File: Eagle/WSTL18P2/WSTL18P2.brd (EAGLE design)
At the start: 23.2 x 23.2 mm, 22 parts, among them CON1 1X6CONN-1.27-ROUND, CON2 1X6CONN-1.27-ROUND, CON3 1X6CONN-1.27-ROUND, CON4 1X6CONN-1.27-ROUND, T1 ABS07AIG

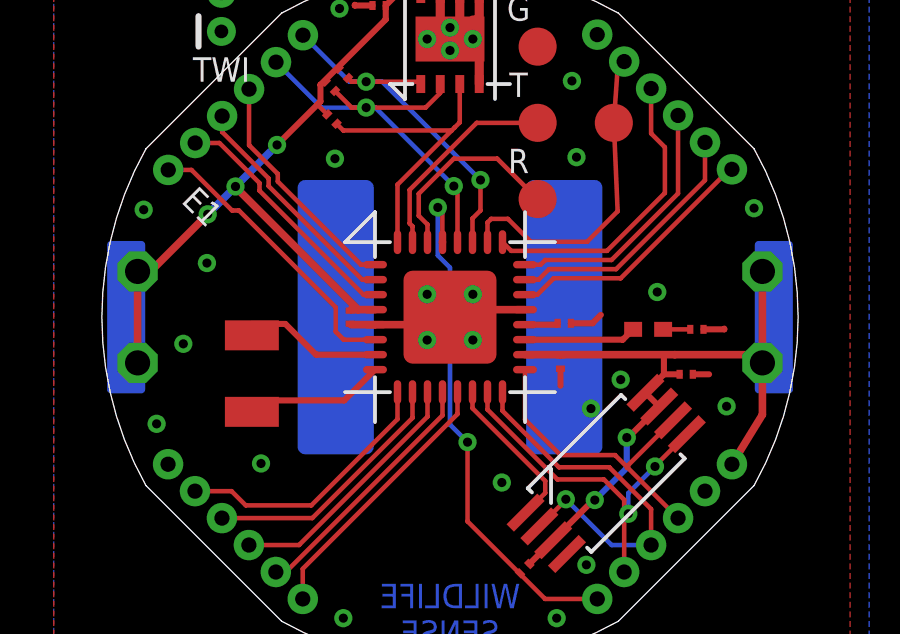
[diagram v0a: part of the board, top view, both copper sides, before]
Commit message: Moved battery GND pad to a sincle circular in centre
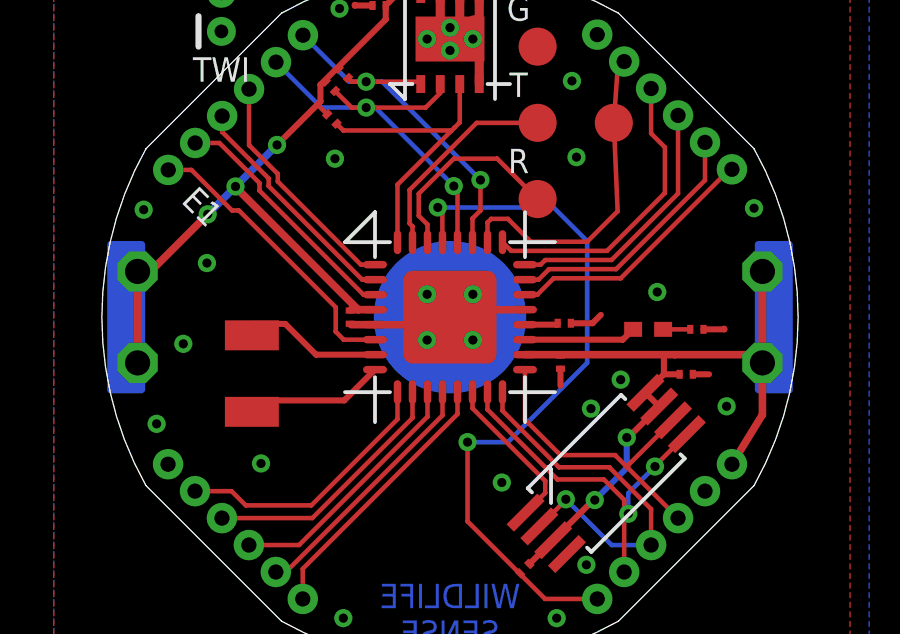
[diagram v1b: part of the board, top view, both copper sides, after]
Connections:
- net GND: no longer U$1.GND1
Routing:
- net RESET: track 17.5 -> 23.9 mm
- net GND: track 15.5 -> 16.1 mm
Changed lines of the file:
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@@
 <wire x1="12.954" y1="15.712" x2="12.954" y2="16.7132" width="0.1524" layer="1"/>
 <via x="12.8016" y="16.8656" extent="1-16" drill="0.3048" shape="octagon"/>
-<wire x1="12.8016" y1="15.2654" x2="13.208" y2="14.859" width="0.1524" layer="16"/>
-<wire x1="12.8016" y1="15.2654" x2="12.8016" y2="16.8656" width="0.1524" layer="16"/>
 <wire x1="12.954" y1="16.7132" x2="12.8016" y2="16.8656" width="0.1524" layer="1"/>
 <wire x1="13.7922" y1="6.4008" x2="15.541634375" y2="4.651365625" width="0.1524" layer="1"/>
@@
 <wire x1="18.115871875" y1="3.815671875" x2="16.377328125" y2="3.815671875" width="0.1524" layer="1"/>
 <wire x1="15.541634375" y1="4.670434375" x2="15.541634375" y2="4.651365625" width="0.1524" layer="1"/>
-<wire x1="13.208" y1="14.859" x2="13.208" y2="9.6266" width="0.1524" layer="16"/>
-<wire x1="13.208" y1="9.6266" x2="13.7922" y2="9.0424" width="0.1524" layer="16"/>
 <via x="13.7922" y="9.0424" extent="1-16" drill="0.3048" shape="octagon"/>
 <wire x1="13.7922" y1="9.0424" x2="13.7922" y2="6.4008" width="0.1524" layer="1"/>
+<wire x1="12.8016" y1="16.8656" x2="16.6624" y2="16.8656" width="0.1524" layer="16"/>
+<wire x1="16.6624" y1="16.8656" x2="17.78" y2="15.748" width="0.1524" layer="16"/>
+<wire x1="17.78" y1="15.748" x2="17.78" y2="11.684" width="0.1524" layer="16"/>
+<wire x1="17.78" y1="11.684" x2="15.1384" y2="9.0424" width="0.1524" layer="16"/>
+<wire x1="15.1384" y1="9.0424" x2="13.7922" y2="9.0424" width="0.1524" layer="16"/>
 </signal>
 <signal name="VCC">
@@
 <contactref element="MCU" pad="PAD"/>
 <wire x1="10.708" y1="12.958" x2="12.446" y2="12.958" width="0.254" layer="1"/>
-<wire x1="12.446" y1="12.958" x2="12.446" y2="12.446" width="0.254" layer="1"/>
 <wire x1="13.97" y1="13.458" x2="13.97" y2="13.97" width="0.254" layer="1"/>
 <via x="6.9088" y="8.3312" extent="1-16" drill="0.3048"/>
@@
 <via x="14.9352" y="7.6962" extent="1-16" drill="0.3048"/>
 <via x="5.1054" y="15.0114" extent="1-16" drill="0.3048"/>
-<contactref element="U$1" pad="GND1"/>
 <contactref element="U$1" pad="GND"/>
 <via x="9.525" y="23.495" extent="1-16" drill="0.3048"/>
@@
 <wire x1="22.352" y1="12.8016" x2="22.352" y2="12.827" width="0.2032" layer="1"/>
 <wire x1="15.708" y1="13.458" x2="13.97" y2="13.458" width="0.254" layer="1"/>
+<wire x1="13.208" y1="13.208" x2="12.446" y2="12.446" width="0.4064" layer="16"/>
+<wire x1="13.208" y1="13.208" x2="13.97" y2="13.458" width="0" layer="19" extent="1-16"/>
+<wire x1="13.208" y1="13.208" x2="13.208" y2="13.208" width="0" layer="19" extent="1-16"/>
+<wire x1="12.446" y1="13.97" x2="12.696" y2="13.208" width="0" layer="19" extent="1-1"/>
+<wire x1="13.97" y1="12.446" x2="13.97" y2="13.458" width="0" layer="19" extent="1-1"/>
 </signal>
 <signal name="AREF">

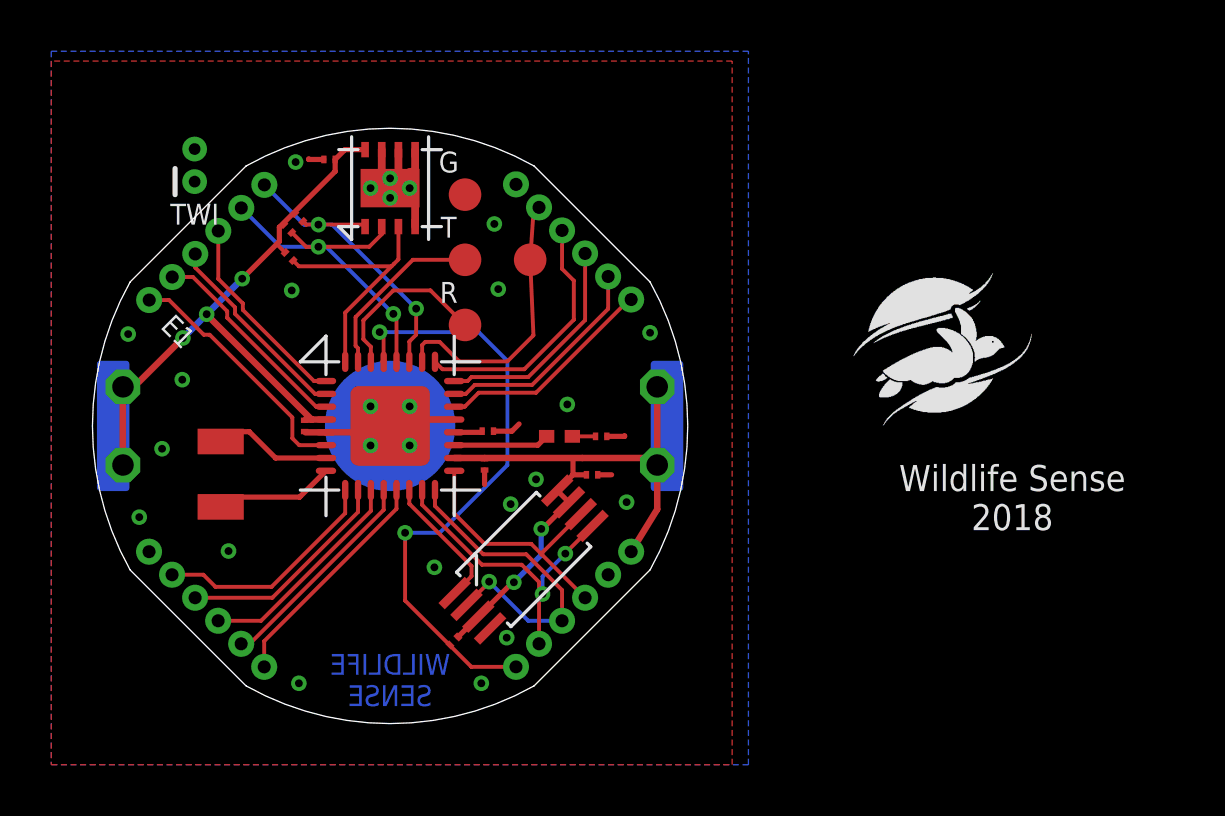
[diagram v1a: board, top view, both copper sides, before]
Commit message: Reverted some passives back to 0402 size
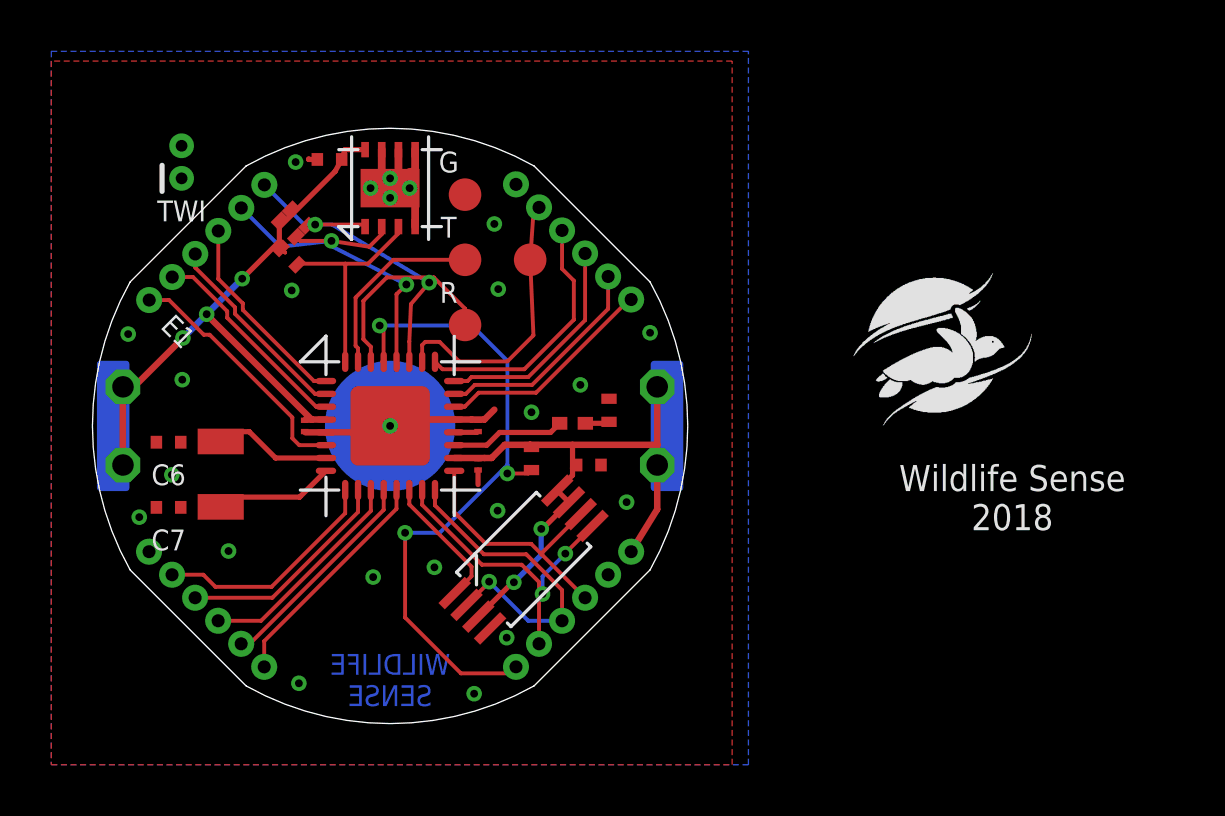
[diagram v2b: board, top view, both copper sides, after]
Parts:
- added C6, C7: CAP_0402_CERAMIC, Passives:CAP_0402
- C4, C5: device Passives:RES_CAP_0201 -> Passives:CAP_0402
- R1, R2, R3, R4, R5: device Passives:RES_CAP_0201 -> Passives:RES_0402
- moved R1 7.73 mm to (18.7, 11.9), turned to 270 degrees
- moved R5 1.06 mm to (21.7, 13.8), turned to 90 degrees
- moved LED0 0.72 mm to (20.3, 13.3)
- moved TWI 0.52 mm to (5.08, 22.9)
- moved C3 0.43 mm to (16.6, 13.2), turned to 90 degrees
- moved C5 0.40 mm to (21.0, 11.7)
- moved C2 0.25 mm to (16.6, 11.7)
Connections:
- net GND: now also C6.2, C7.2
- net N$1: now also C7.1
- net N$2: now also C6.1
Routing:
- net RESET: track 23.9 -> 26.1 mm, vias 2 -> 3
- net TMP_INT: track 10.1 -> 8.62 mm
- net GND: track 16.1 -> 14.8 mm, vias 26 -> 24
- net RXD0: track 6.74 -> 7.98 mm
- net SCL0: track 13.8 -> 14.7 mm
- net SDA0: track 12.6 -> 13.4 mm
- net PE2: track 3.75 -> 4.46 mm
- net VCC: track 49.0 -> 48.3 mm

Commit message: Removed WP and HOLD connections to VCC on EEPROM
Chip has internal pull-ups for when WP and HOLD functions are not used
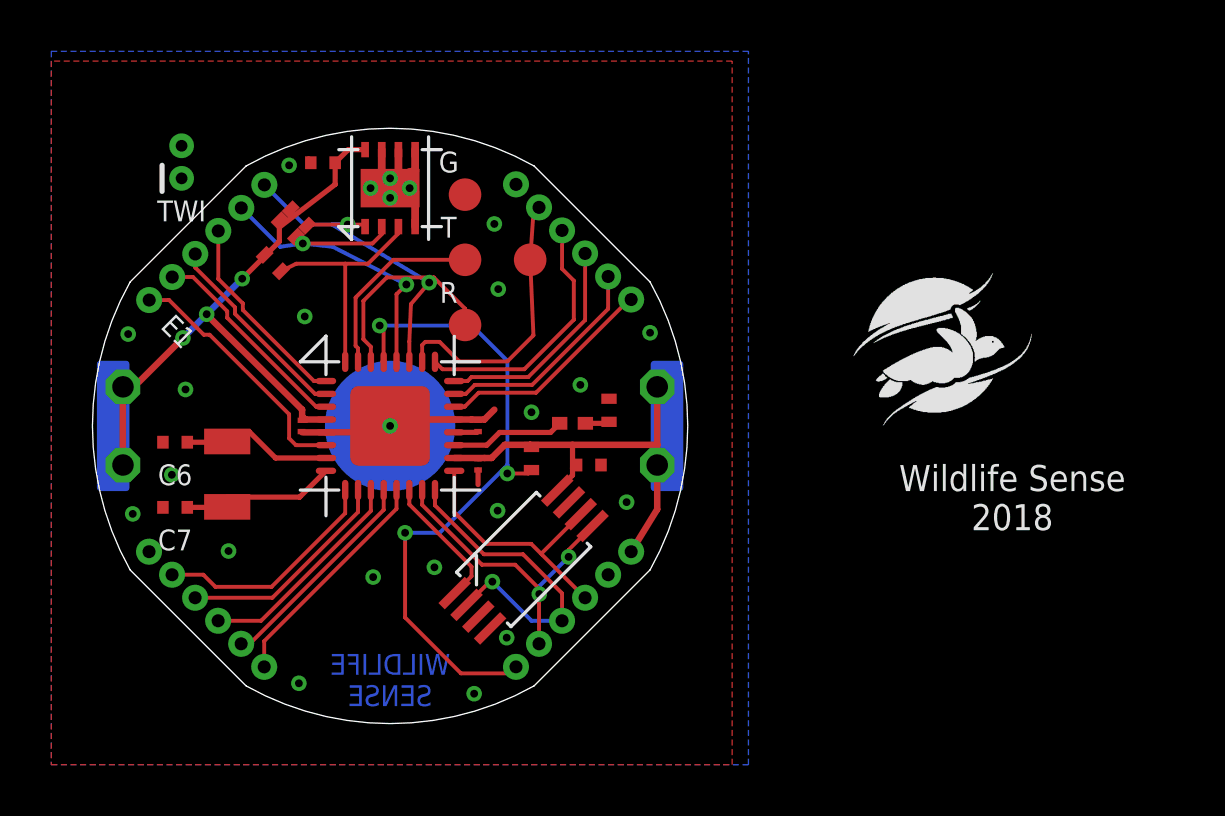
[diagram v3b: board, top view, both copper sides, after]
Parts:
- moved R4 0.68 mm to (8.64, 19.6)
- moved C4 0.28 mm to (10.6, 23.5)
- moved C6 0.25 mm to (4.83, 12.6)
- moved C7 0.25 mm to (4.83, 10.0)
- moved T1 0.25 mm to (6.86, 11.3)
- moved C1 0.13 mm to (9.75, 13.2)
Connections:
- net VCC: no longer MEM.3, MEM.7
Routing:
- net VCC: track 48.3 -> 41.3 mm, vias 5 -> 3
- net N$2: track 4.91 -> 6.22 mm
- net N$1: track 4.91 -> 6.22 mm
- net SDA0: track 13.4 -> 14.6 mm
- net TMP_INT: track 8.62 -> 9.22 mm

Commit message: Rerouted TWI (I2C)
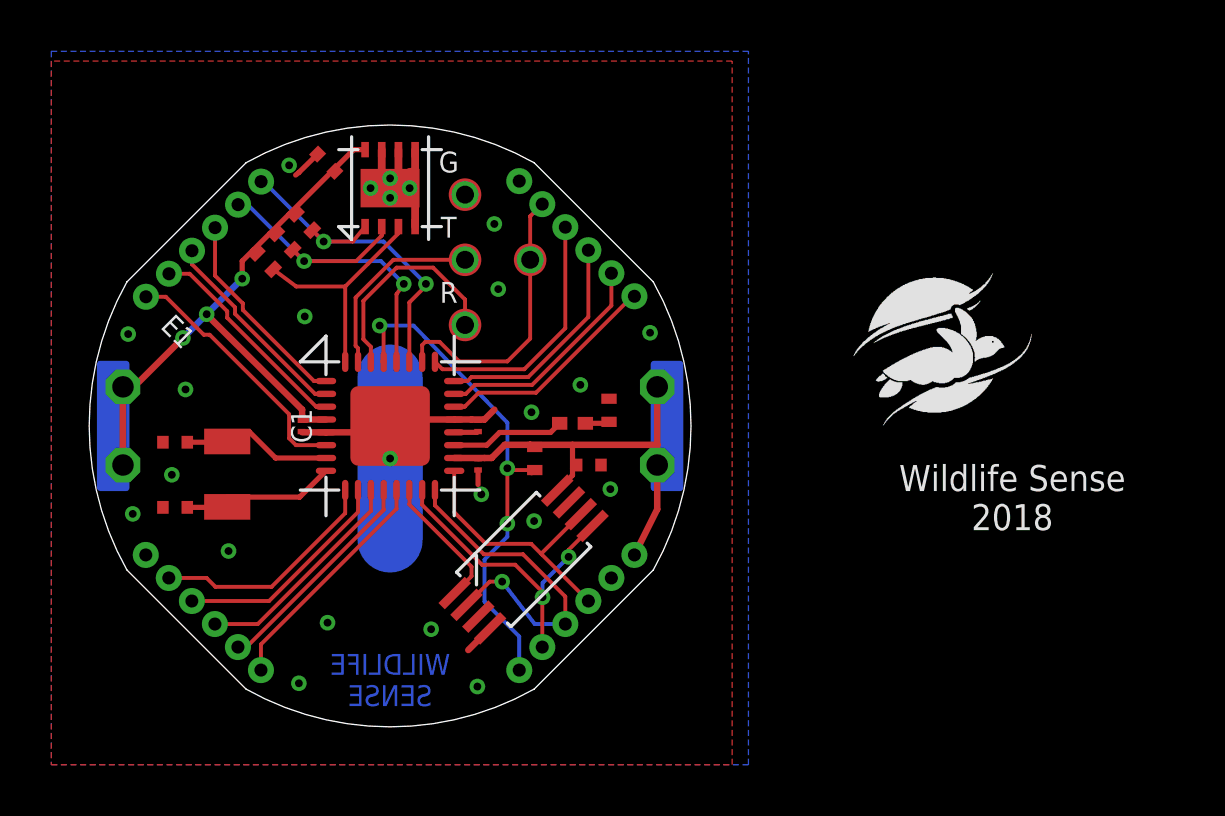
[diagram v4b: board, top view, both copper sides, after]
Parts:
- removed TWI: 1X2CONN1.27, AVR_ISP_127:1X2_1.27
- moved R3 0.52 mm to (9.09, 20.4)
- moved R4 0.31 mm to (8.33, 19.6)
- moved R2 0.27 mm to (9.86, 21.2)
- moved CON2 0.18 mm to (3.68, 8.18)
- moved CON1 0.18 mm to (22.7, 8.18)
- moved CON3 0.18 mm to (22.7, 18.3)
- moved CON4 0.18 mm to (8.18, 22.7)
- moved R1 0.13 mm to (18.8, 11.9)
- moved C4 0.13 mm to (10.7, 23.5), turned to 135 degrees
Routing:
- net RESET: track 26.1 -> 19.9 mm
- net VCC: track 41.3 -> 45.6 mm
- net GND: track 14.7 -> 18.8 mm, vias 24 -> 25
- net SCL0: track 14.5 -> 15.6 mm
- net SDA0: track 14.6 -> 13.9 mm
- net RXD0: track 7.98 -> 8.50 mm, vias 0 -> 1
- net PC3: track 10.9 -> 11.0 mm, vias 0 -> 1
- net TXD0: vias 0 -> 1
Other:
- board size 23.2 x 23.2 mm -> 23.5 x 23.5 mm

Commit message: Eliminated all 0201 passives, changed uart connection pin
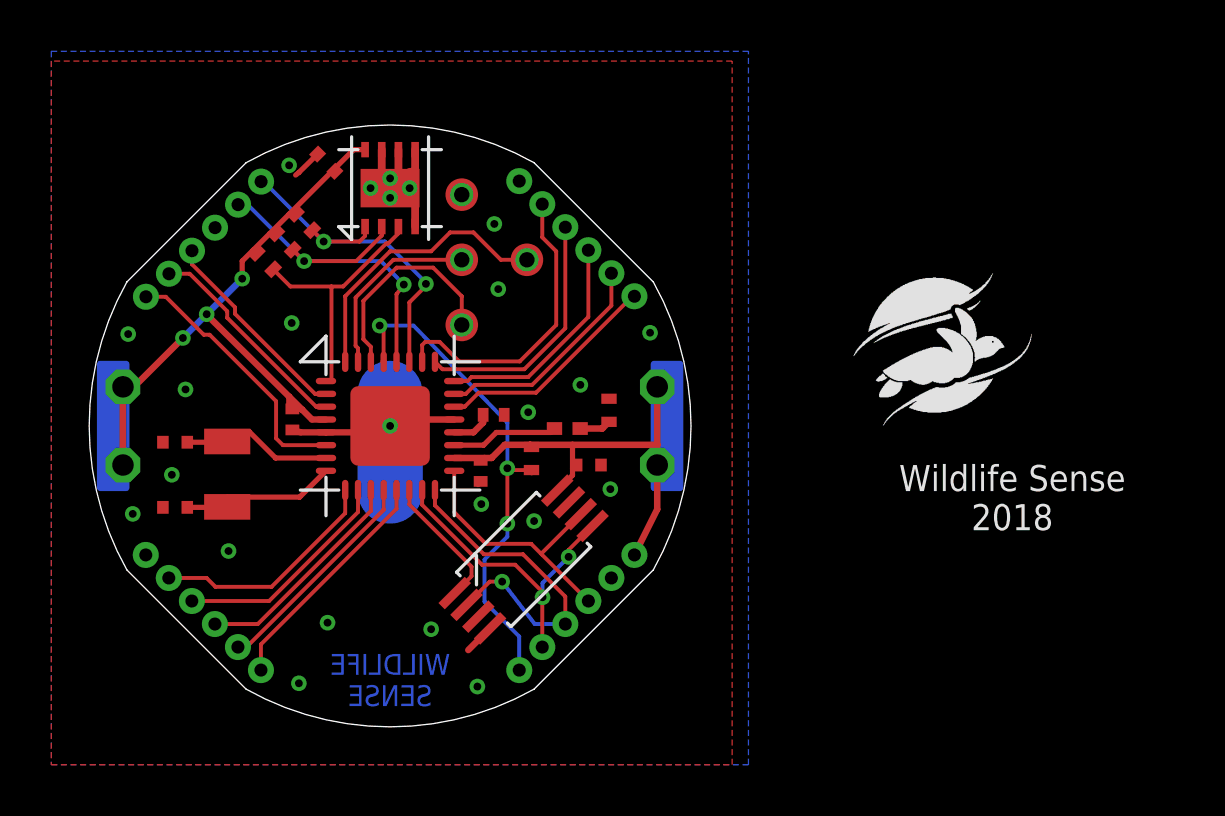
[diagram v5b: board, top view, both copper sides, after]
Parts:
- C1, C2, C3: device Passives:RES_CAP_0201 -> Passives:SMD_0402
- moved C3 0.75 mm to (17.2, 13.6)
- moved C1 0.44 mm to (9.40, 13.5), turned to 0 degrees
- moved LED0 0.29 mm to (20.1, 13.1)
- moved C2 0.27 mm to (16.7, 11.5), turned to 0 degrees
- moved R1 0.13 mm to (18.7, 11.9)
- moved UART 0.13 mm to (16.0, 17.1)
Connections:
- removed net PD3: CON4.3, MCU.1
- new net PD2: MCU.32, UART.1
- new net UNKN1: CON4.3
- net PC3: no longer UART.1
- net TMP_INT: now also MCU.1; no longer MCU.32
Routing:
- net PD2: track 0.00 -> 11.1 mm, vias 0 -> 1
- net PD3: track 8.05 -> 0.00 mm
- net GND: track 18.8 -> 14.7 mm
- net TMP_INT: track 9.16 -> 10.2 mm
- net PC3: track 11.0 -> 11.8 mm, vias 1 -> 0
- net AREF: track 0.94 -> 1.59 mm
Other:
- board text removed: "E1"
- board text removed: "G"
- board text removed: "R"
- board text removed: "T"

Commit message: Chaned LED pin, added VCC and GND next to TWI(I2C) headers, changed some traces to 8mil
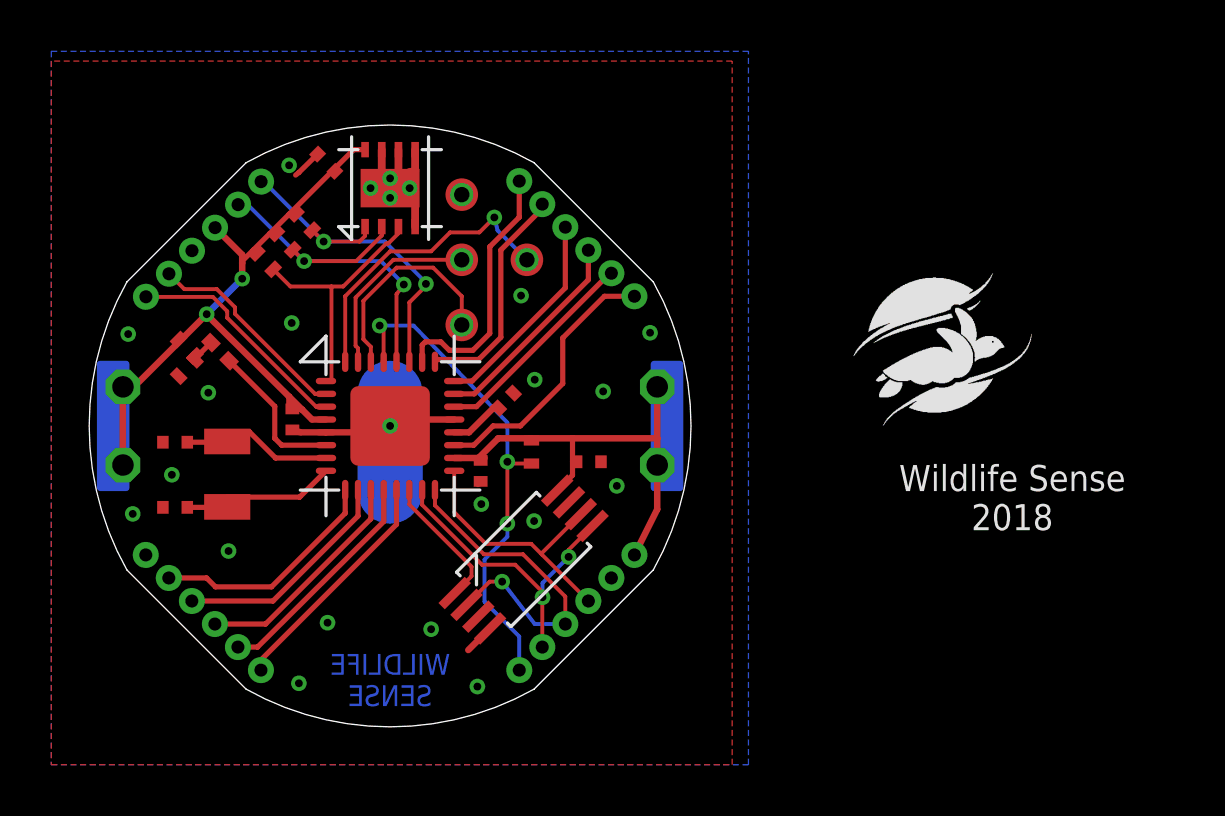
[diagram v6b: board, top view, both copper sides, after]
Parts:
- added R6: 1k, Passives:RES_0402
- moved R5 16.5 mm to (5.28, 15.5), turned to 225 degrees
- moved LED0 13.9 mm to (6.58, 16.1), turned to 135 degrees
- moved C3 0.74 mm to (17.7, 14.2), turned to 135 degrees
- moved R1 0.25 mm to (18.7, 12.2)
- moved C5 0.13 mm to (21.0, 11.8)
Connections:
- removed net UNKN1: CON4.3
- net GND: now also CON4.4; no longer CON3.6
- net N$4: now also R6.1
- net PC0: now also CON3.3; no longer CON3.2
- net PC1: now also CON3.4; no longer CON3.3
- net PC2: now also CON3.5; no longer CON3.4
- net PC3: now also CON3.6; no longer CON3.5
- net PD4: now also CON4.5; no longer CON4.4
- net PE0: now also CON4.6; no longer CON4.5
- net PE1: now also LED0.ANODE; no longer CON4.6
- net PE2: now also CON3.1; no longer LED0.ANODE
- net PE3: now also CON3.2; no longer CON3.1
- net VCC: now also CON4.3, R6.2
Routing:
- net PE2: track 4.18 -> 10.5 mm
- net PE1: track 10.3 -> 5.87 mm
- net VCC: track 45.7 -> 48.2 mm, vias 3 -> 2
- net PC3: track 11.8 -> 10.2 mm
- net PC2: track 9.80 -> 8.82 mm
- net PD2: track 11.1 -> 11.8 mm, vias 1 -> 2
- net PC1: track 8.87 -> 8.20 mm
- net PC0: track 8.81 -> 8.22 mm
- net AREF: track 1.59 -> 2.13 mm
- net PE0: track 8.42 -> 8.94 mm
- net PE3: track 8.79 -> 8.28 mm
- net GND: vias 25 -> 24
